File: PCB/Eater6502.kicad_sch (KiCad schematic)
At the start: 3 parts, among them SW1 SW_Push_SPDT, U1 W65C02S

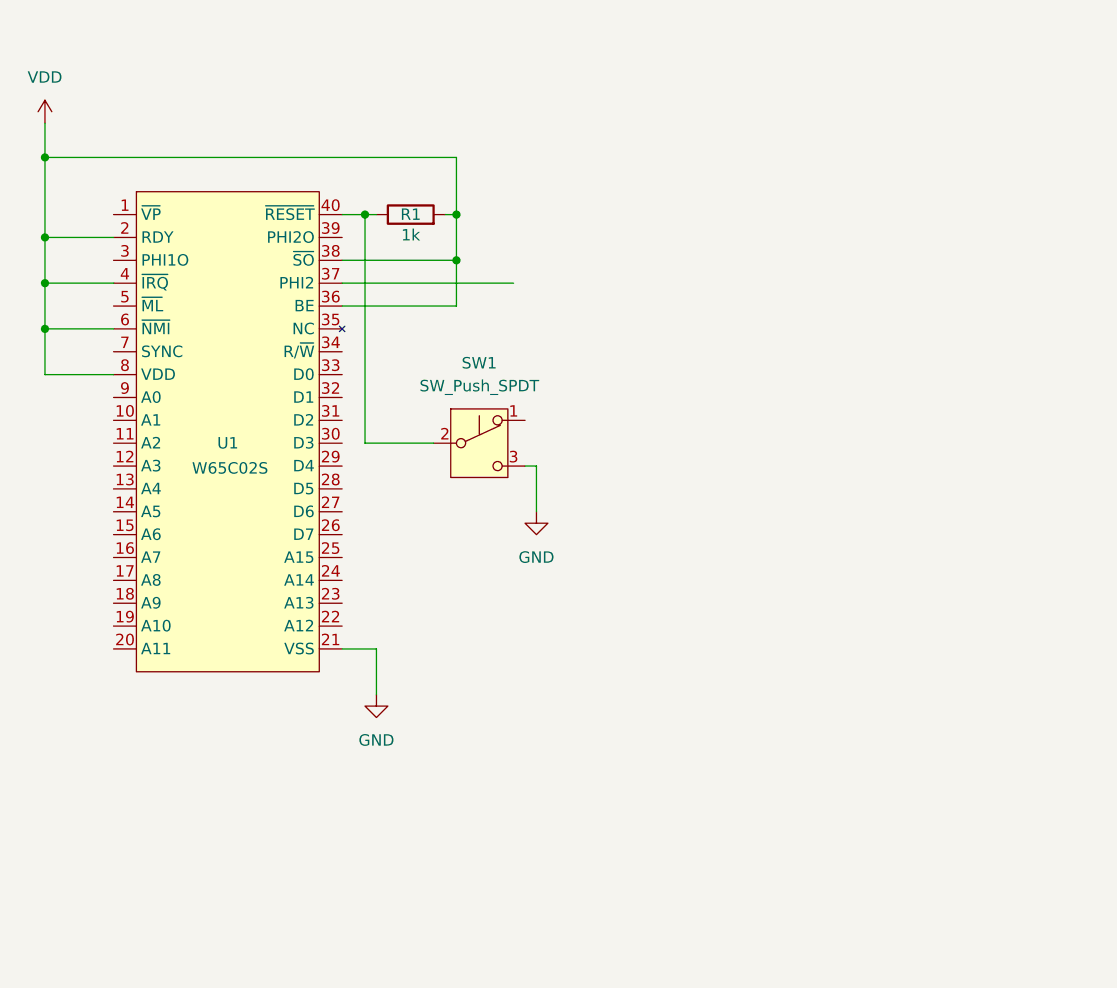
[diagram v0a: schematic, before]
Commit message: Working debugger and firmware for store to address
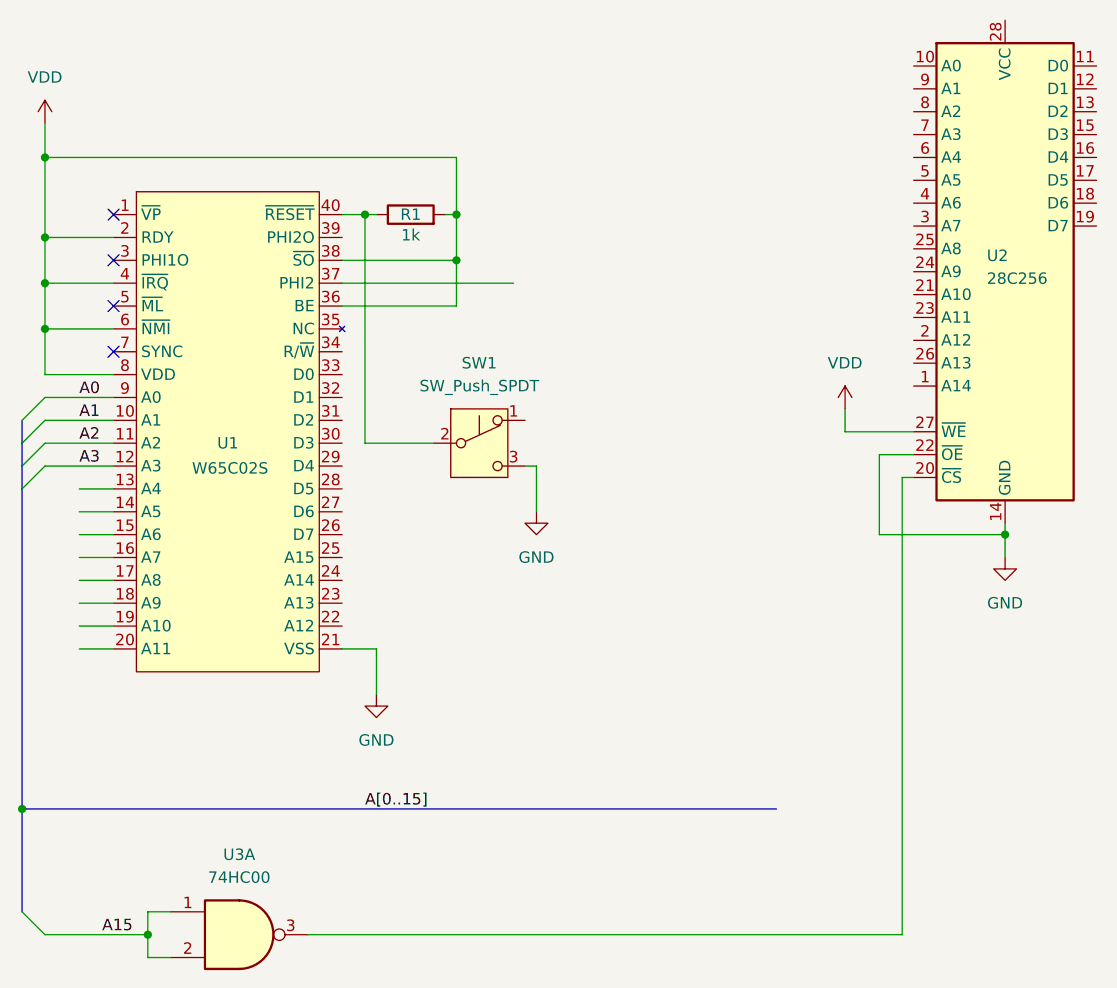
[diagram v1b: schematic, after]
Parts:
- added U2: 28C256, symbol Memory_EEPROM:28C256
- added U3: 74HC00, symbol 74xx:74HC00
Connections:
- net GND: now also U2.14 (GND), U2.22 (~{OE})
- net VDD: now also U2.27 (~{WE})
- net A1: now reaches U1.10 (A1)
- net A2: now reaches U1.11 (A2)
- net A3: now reaches U1.12 (A3)
- net A0: now reaches U1.9 (A0)
- new net: U2.20 (~{CS}), U3.3
- new net A15: U3.1, U3.2
- no-connect marks 0 -> 4

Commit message: ...
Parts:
- removed SW1: SW_Push_SPDT, symbol Switch:SW_Push_SPDT
- removed U3: 74HC00, symbol 74xx:74HC00
- added C1: 0.1u, symbol Device:C
- added R2: 1k, symbol Device:R
- added SW1: Reset, symbol Switch:SW_Push
- added U3: 74HC00, Package_DIP:DIP-14_W7.62mm_LongPads, symbol 74xx:74HC00
- added U4: W65C22SxP, Package_DIP:DIP-40_W15.24mm, symbol PCM_65xx-library:W65C22SxP
- U1: footprint (none) -> Package_DIP:DIP-40_W15.24mm_LongPads
- U2: footprint (none) -> Package_DIP:DIP-28_W15.24mm_Socket_LongPads
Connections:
- net A0: now also U2.10 (A0), U4.35 (RS3)
- net A1: now also U2.9 (A1), U4.36 (RS2)
- net A15: now also U1.25 (A15), U3.12, U3.13
- net A2: now also U2.8 (A2), U4.37 (RS1)
- net A3: now also U2.7 (A3), U4.38 (RS0)
- net GND: now also C1.2, SW1.1, U3.7 (GND), U4.1 (VSS)
- net at U1.40 (~{RESET}): now also R1.2, C1.1, SW1.2, U4.34 (~{RES}); no longer R1.1
- net A4: now reaches U1.13 (A4)
- net A4: now also U2.6 (A4)
- net A5: now reaches U1.14 (A5)
- net A5: now also U2.5 (A5)
- net A6: now reaches U1.15 (A6)
- net A6: now also U2.4 (A6)
- net A7: now reaches U1.16 (A7)
- net A7: now also U2.3 (A7)
- net A8: now reaches U1.17 (A8)
- net A8: now also U2.25 (A8)
- net A9: now reaches U1.18 (A9)
- net A9: now also U2.24 (A9)
- net A10: now reaches U1.19 (A10)
- net A10: now also U2.21 (A10)
- net A11: now reaches U1.20 (A11)
- net A11: now also U2.23 (A11)
- net A12: now reaches U1.22 (A12)
- net A12: now also U2.2 (A12)
- net A13: now reaches U1.23 (A13)
- net A13: now also U2.26 (A13), U4.24 (CS1)
- net A14: now reaches U1.24 (A14)
- net A14: now also U2.1 (A14), U3.4
- net D7: now reaches U1.26 (D7)
- net D7: now also U2.19 (D7), U4.26 (D7)
- net D6: now reaches U1.27 (D6)
- net D6: now also U2.18 (D6), U4.27 (D6)
- net D5: now reaches U1.28 (D5)
- net D5: now also U2.17 (D5), U4.28 (D5)
- net D4: now reaches U1.29 (D4)
- net D4: now also U2.16 (D4), U4.29 (D4)
- net D3: now reaches U1.30 (D3)
- net D3: now also U2.15 (D3), U4.30 (D3)
- net D2: now reaches U1.31 (D2)
- net D2: now also U2.13 (D2), U4.31 (D2)
- net D1: now reaches U1.32 (D1)
- net D1: now also U2.12 (D1), U4.32 (D1)
- net D0: now reaches U1.33 (D0)
- net D0: now also U2.11 (D0), U4.33 (D0)
- net at U1.34 (R/~{W}): now also U4.22 (R/~{W})
- net clock: now reaches U1.37 (PHI2)
- net clock: now also U4.25 (ϕ2)
- net at U2.20 (~{CS}): now also U3.11, U3.5
- net +5V: now reaches U2.28 (VCC)
- net +5V: now also R1.1, U1.36 (BE), U1.38 (~{SO}), U1.4 (~{IRQ}), U1.6 (~{NMI}), U1.8 (VDD), U2.27 (~{WE}), R2.1, U3.14 (VCC), U4.20 (VCC)
- removed net VDD: R1.2, U1.2 (RDY), U1.36 (BE), U1.38 (~{SO}), U1.4 (~{IRQ}), U1.6 (~{NMI}), U1.8 (VDD), U2.27 (~{WE})
- new net: U3.6, U4.23 (~{CS2})
- new net: R2.2, U1.2 (RDY)
- no-connect marks 4 -> 9
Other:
- added sheet arduino-shield (arduino_shield.kicad_sch)
- moved on the sheet: R1, U1, U2
